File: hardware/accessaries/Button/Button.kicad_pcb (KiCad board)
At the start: 2 copper layers, 36 x 48 mm, 22 parts, among them P1 IO_HOLE-3.2, P2 IO_HOLE-3.2, P3 IO_HOLE-3.2, P4 IO_HOLE-3.2, P5 IO_HOLE-3.2, P6 IO_HOLE-3.2, P7 IO_HOLE-3.2, P8 IO_HOLE-3.2

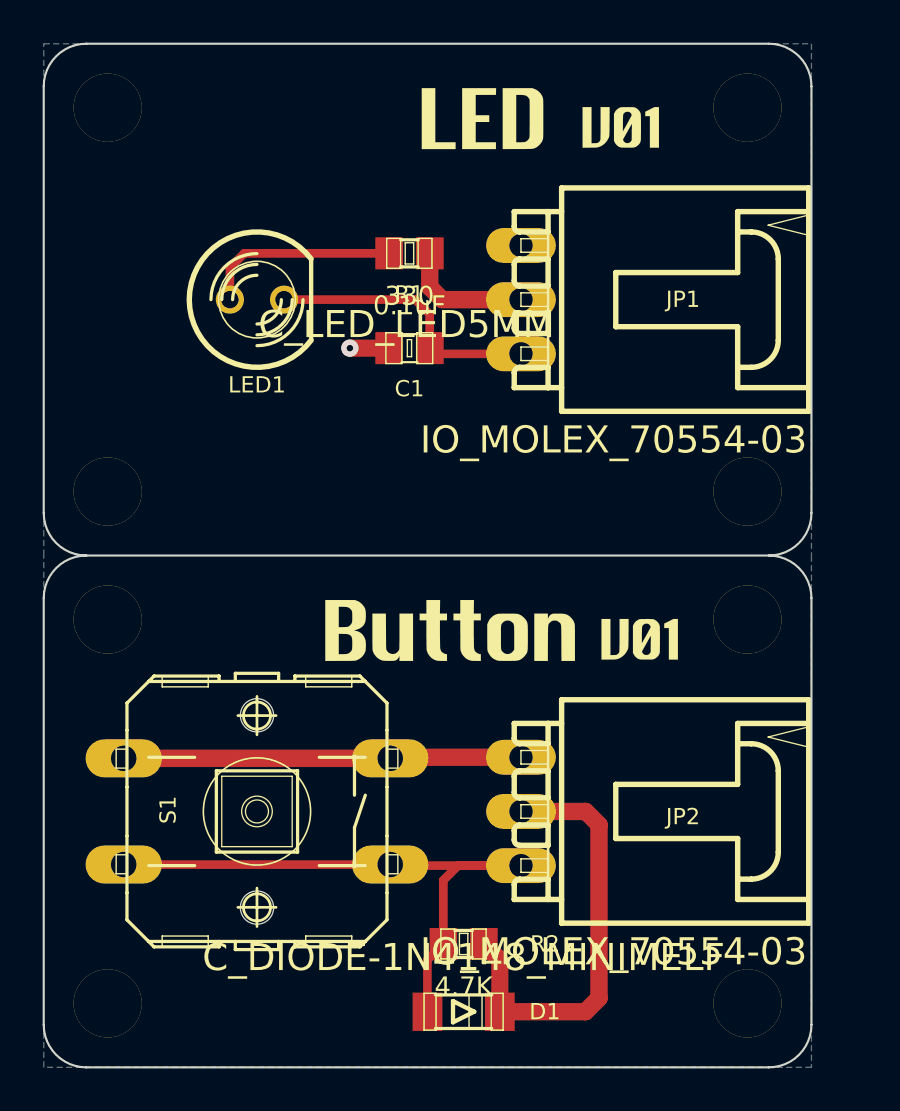
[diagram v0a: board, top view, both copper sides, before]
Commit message: Separate into two modules
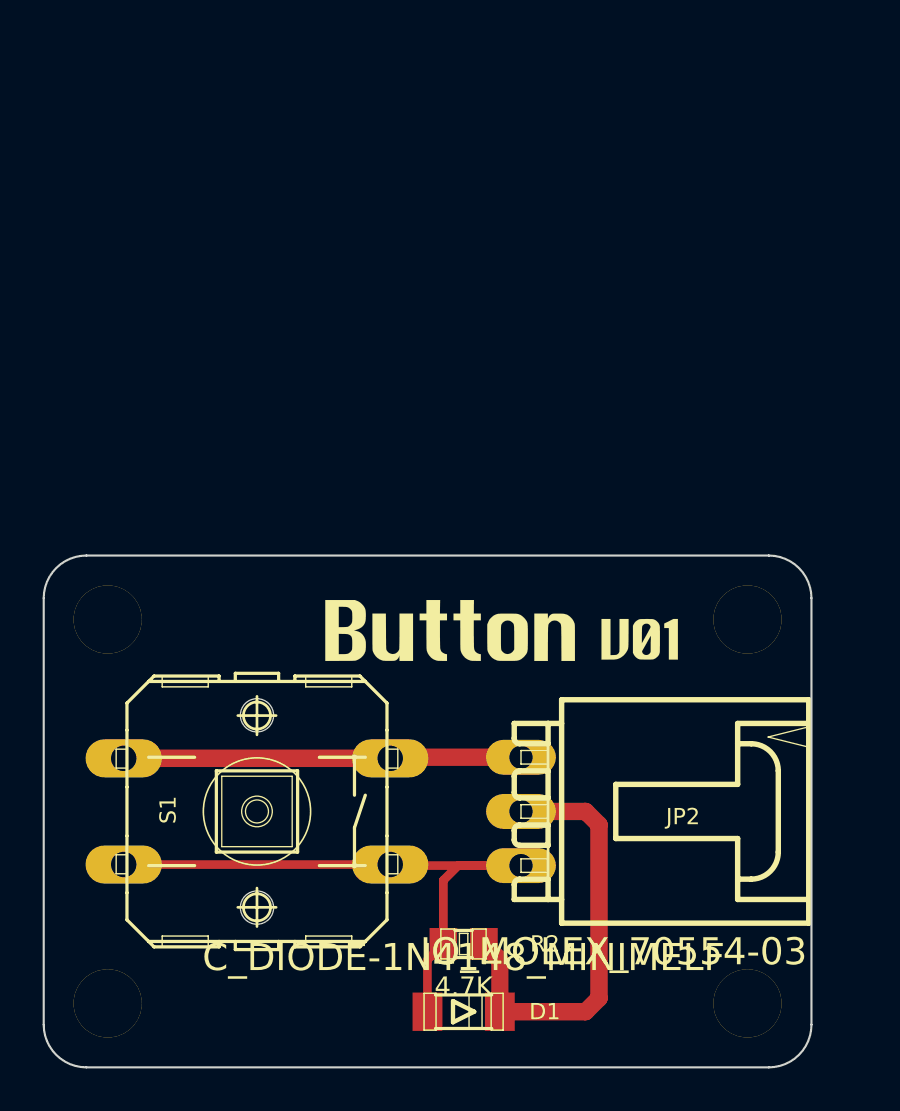
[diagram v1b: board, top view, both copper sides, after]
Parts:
- removed C1: 0.1uF, C_C_0805
- removed the G*** at (60.6, 31.0)
- removed the G*** at (67.1, 31.2)
- removed JP1: IO_MOLEX_70554-03, IO_MOLEX_70554-03
- removed LED1: C_LED_LED5MM, C_LED_LED5MM
- removed P1, P2, P3, P4: IO_HOLE-3.2, IO_HOLE-3.2
- removed R1: 330, C_R_0805
- removed the VAL at (56.0, 39.0)
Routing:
- net N-000004: track 13.1 -> 0.00 mm
- net N-000002: track 9.25 -> 0.00 mm
- net +3.3V: track 26.6 -> 20.4 mm
- net GND: track 20.5 -> 18.6 mm, vias 1 -> 0
- removed copper zone on B.Cu, net GND
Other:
- board size 36 x 48 mm -> 36 x 24 mm
